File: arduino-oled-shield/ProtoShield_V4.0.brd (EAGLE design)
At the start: 68.6 x 53.3 mm, 22 parts

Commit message: making changes for arduino
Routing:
- net N$37: track 45.8 -> 43.3 mm
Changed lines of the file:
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@@
 <wire x1="48.75" y1="21.5" x2="45.25" y2="21.5" width="0.4064" layer="16"/>
 <wire x1="45.25" y1="21.5" x2="43.75" y2="20" width="0.4064" layer="16"/>
-<wire x1="43.75" y1="20" x2="43.75" y2="13" width="0.4064" layer="16"/>
-<wire x1="43.75" y1="13" x2="41.75" y2="11" width="0.4064" layer="16"/>
-<wire x1="41.75" y1="11" x2="25.75" y2="11" width="0.4064" layer="16"/>
-<wire x1="25.75" y1="11" x2="24.25" y2="12.5" width="0.4064" layer="16"/>
-<wire x1="24.25" y1="12.5" x2="24.25" y2="19.63" width="0.4064" layer="16"/>
+<wire x1="43.75" y1="20" x2="43.75" y2="14.25" width="0.4064" layer="16"/>
+<wire x1="43.75" y1="14.25" x2="41.75" y2="12.25" width="0.4064" layer="16"/>
+<wire x1="41.75" y1="12.25" x2="25.75" y2="12.25" width="0.4064" layer="16"/>
+<wire x1="25.75" y1="12.25" x2="24.25" y2="13.75" width="0.4064" layer="16"/>
+<wire x1="24.25" y1="13.75" x2="24.25" y2="19.63" width="0.4064" layer="16"/>
 <wire x1="24.25" y1="19.63" x2="24.31" y2="19.69" width="0.4064" layer="16"/>
 </signal>

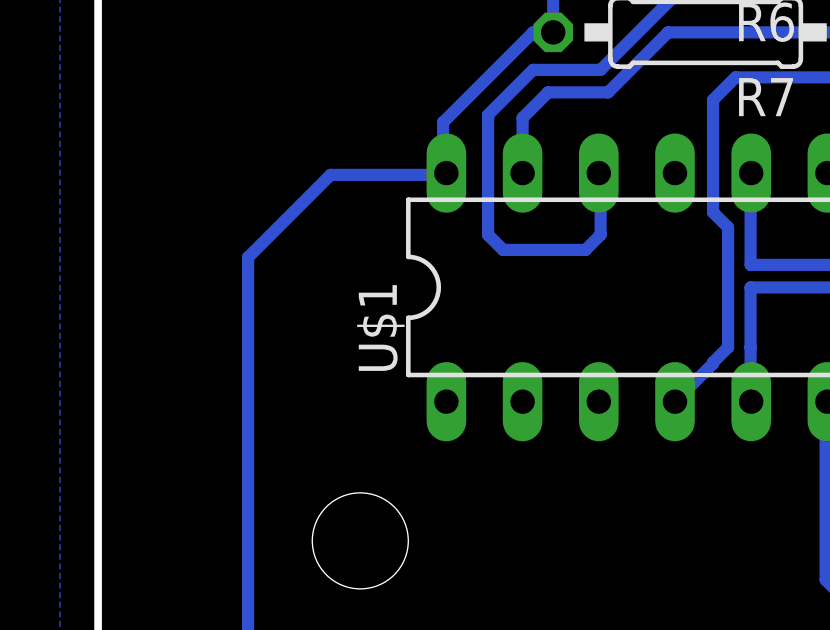
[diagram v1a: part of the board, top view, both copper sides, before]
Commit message: slow getButtonsNoneBlocking fixed, read analog only when used, popFromACC
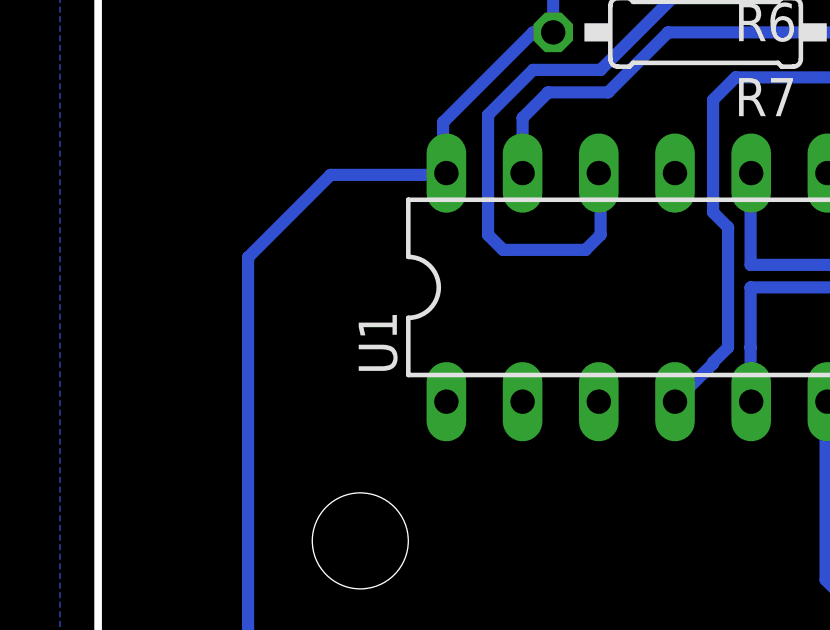
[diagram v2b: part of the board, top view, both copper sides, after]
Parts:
- renumbered U$1 to U1
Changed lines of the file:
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@@
 <layer number="59" name="tCarbon" color="7" fill="1" visible="no" active="no"/>
 <layer number="60" name="bCarbon" color="7" fill="1" visible="no" active="no"/>
-<layer number="88" name="SimResults" color="9" fill="1" visible="no" active="yes"/>
-<layer number="89" name="SimProbes" color="9" fill="1" visible="no" active="yes"/>
+<layer number="88" name="SimResults" color="9" fill="1" visible="yes" active="yes"/>
+<layer number="89" name="SimProbes" color="9" fill="1" visible="yes" active="yes"/>
 <layer number="90" name="Modules" color="5" fill="1" visible="no" active="no"/>
 <layer number="91" name="Nets" color="2" fill="1" visible="no" active="no"/>
@@
 <attribute name="MPN" value="" x="36.83" y="5.08" size="1.778" layer="27" display="off"/>
 </element>
-<element name="U$1" library="pcf8574p" package="DIL16" value="PCF8574P" x="20.5" y="23.5"/>
+<element name="U1" library="pcf8574p" package="DIL16" value="PCF8574P" x="20.5" y="23.5"/>
 <element name="S1" library="switch-omron" package="B3F-10XX" value="" x="50" y="35.5">
 <attribute name="OC_NEWARK" value="36M3542" x="50" y="35.5" size="1.778" layer="27" display="off"/>
@@
 <contactref element="S4" pad="3"/>
 <contactref element="S5" pad="4"/>
-<contactref element="U$1" pad="2"/>
-<contactref element="U$1" pad="1"/>
-<contactref element="U$1" pad="3"/>
-<contactref element="U$1" pad="8"/>
+<contactref element="U1" pad="2"/>
+<contactref element="U1" pad="1"/>
+<contactref element="U1" pad="3"/>
+<contactref element="U1" pad="8"/>
 <contactref element="J1" pad="1"/>
 <contactref element="POWER1" pad="6"/>
@@
 <wire x1="21.336" y1="48.26" x2="21.336" y2="50.8" width="0.8128" layer="16"/>
 <contactref element="R7" pad="1"/>
-<contactref element="U$1" pad="15"/>
+<contactref element="U1" pad="15"/>
 <contactref element="J1" pad="4"/>
 <wire x1="24.12" y1="38.25" x2="21.336" y2="41.034" width="0.4064" layer="16"/>
@@
 <contactref element="DIGITAL-H1" pad="10"/>
 <wire x1="18.796" y1="48.26" x2="18.796" y2="50.8" width="0.8128" layer="16"/>
-<contactref element="U$1" pad="14"/>
+<contactref element="U1" pad="14"/>
 <contactref element="R6" pad="1"/>
 <contactref element="J1" pad="3"/>
@@
 <contactref element="S1" pad="2"/>
 <contactref element="R1" pad="1"/>
-<contactref element="U$1" pad="4"/>
+<contactref element="U1" pad="4"/>
 <wire x1="53.2512" y1="37.7606" x2="51.2394" y2="37.7606" width="0.4064" layer="16"/>
 <wire x1="51.2394" y1="37.7606" x2="49" y2="40" width="0.4064" layer="16"/>
@@
 <contactref element="S3" pad="1"/>
 <contactref element="R3" pad="1"/>
-<contactref element="U$1" pad="12"/>
+<contactref element="U1" pad="12"/>
 <wire x1="47.7394" y1="23.4988" x2="47.7394" y2="26.2606" width="0.4064" layer="16"/>
 <wire x1="47.7394" y1="26.2606" x2="46.5" y2="27.5" width="0.4064" layer="16"/>
@@
 </signal>
 <signal name="N$37">
-<contactref element="U$1" pad="6"/>
+<contactref element="U1" pad="6"/>
 <contactref element="S5" pad="2"/>
 <wire x1="53.2512" y1="20.2606" x2="49.9894" y2="20.2606" width="0.4064" layer="16"/>
@@
 </signal>
 <signal name="N$33">
-<contactref element="U$1" pad="10"/>
+<contactref element="U1" pad="10"/>
 <contactref element="S4" pad="2"/>
 <wire x1="56.4894" y1="30.0012" x2="56.4894" y2="34.5106" width="0.4064" layer="16"/>
@@
 <contactref element="R4" pad="2"/>
 <contactref element="R5" pad="2"/>
-<contactref element="U$1" pad="16"/>
+<contactref element="U1" pad="16"/>
 <contactref element="R7" pad="2"/>
 <contactref element="R6" pad="2"/>
@@
 </signal>
 <signal name="N$5">
-<contactref element="U$1" pad="5"/>
+<contactref element="U1" pad="5"/>
 <wire x1="21.75" y1="21.5" x2="21.75" y2="19.71" width="0.4064" layer="16"/>
 <wire x1="21.75" y1="19.71" x2="21.77" y2="19.69" width="0.4064" layer="16"/>
